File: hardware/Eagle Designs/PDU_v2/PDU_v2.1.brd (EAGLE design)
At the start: 90.2 x 95.5 mm, 245 parts, among them J1 5037630291, J10 5037630491, J11 UJ31-CH-G1-SMT-TR, J12 5037630291, J13 5037630291, J14 5037630291, J15 5037630291, J16 5037630291, J17 5037630291, J18 5037630491, J19 5037630291, J2 5037630291, J20 503182-1852, J22 5037630291, J23 5037630291, J24 5037630291, J25 5037630291, J27 5037630691, J3 5037630291, J4 5037630291, J5 5037630291, J6 5037630291, J7 5037630491, J8 5037630491, J9 5037630491, M1 BSZ100N06LS3, M2 BSZ100N06LS3, M3 BSZ033NE2LS5, M4 BSZ033NE2LS5, U1 DRV8847PWPR, U10 AO3404A, U11 IRLML2803PBFCT-ND, U12 IRLML2803PBFCT-ND, U13 LT8390EFE#PBF, U14 ATSAME51N19A-AF, U15 INA219BIDR, U16 MIC2514YM5-TR, U17 MAX16998AAUA+T, U18 TMP36FSZ, U2 DRV8847PWPR, U20 AO3404A, U21 LT8609A, U22 LT8609A, U23 BC848ALT1G, U24 AO3404A, U25 SI4835DDY-T1-GE3, U26 SI3493DDV-T1-GE3, U27 SI3493DDV-T1-GE3, U3 LTC1477CS8LINEAR_TECHNOLOGY_L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, U4 LTC1477CS8LINEAR_TECHNOLOGY_L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, U5 LTC1477CS8LINEAR_TECHNOLOGY_L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, U6 LTC1477CS8LINEAR_TECHNOLOGY_L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, U7 LTC1477CS8LINEAR_TECHNOLOGY_L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, U8 LT8609A, U9 LTC1477CS8LINEAR_TECHNOLOGY_L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, Y1 ABS07-32.768KHZ-T

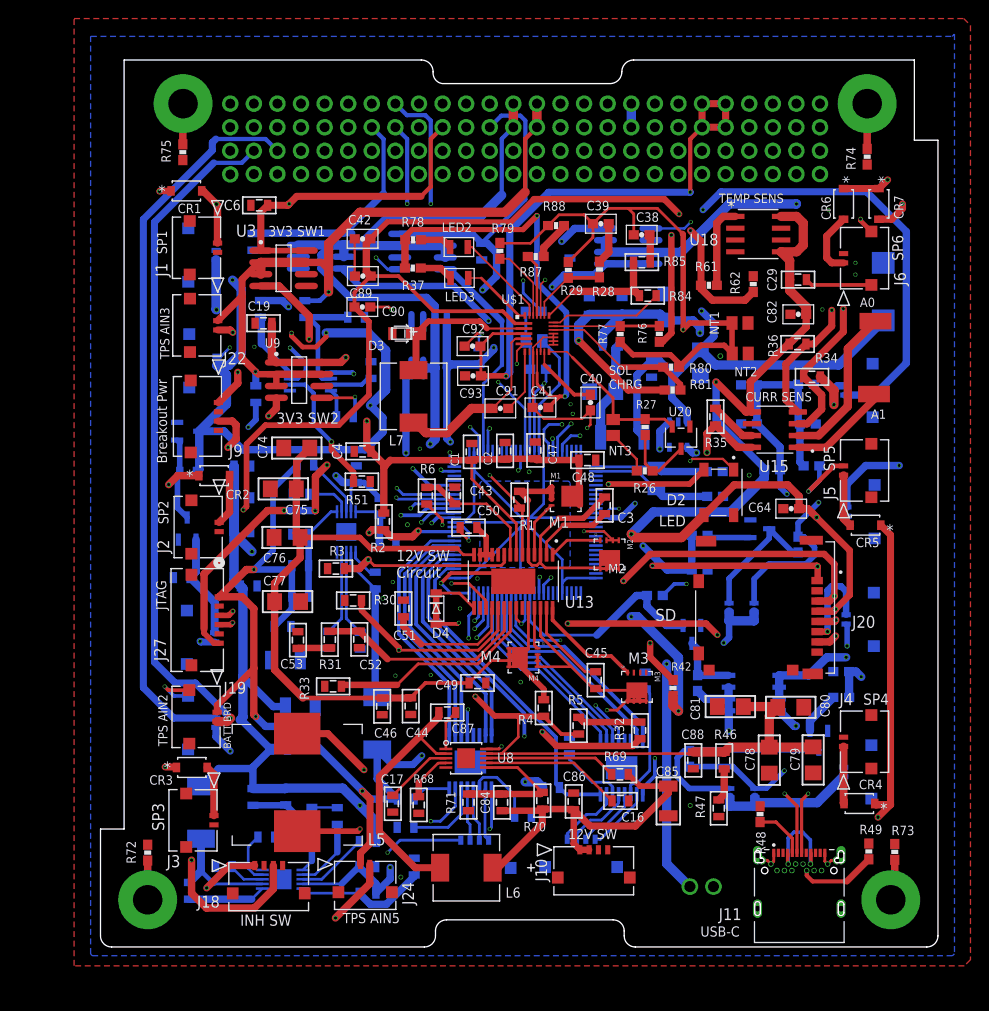
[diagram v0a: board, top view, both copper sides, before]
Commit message: Completed OBC v4.1 (Finished); Updated PDU v2.1 (Unfinished)
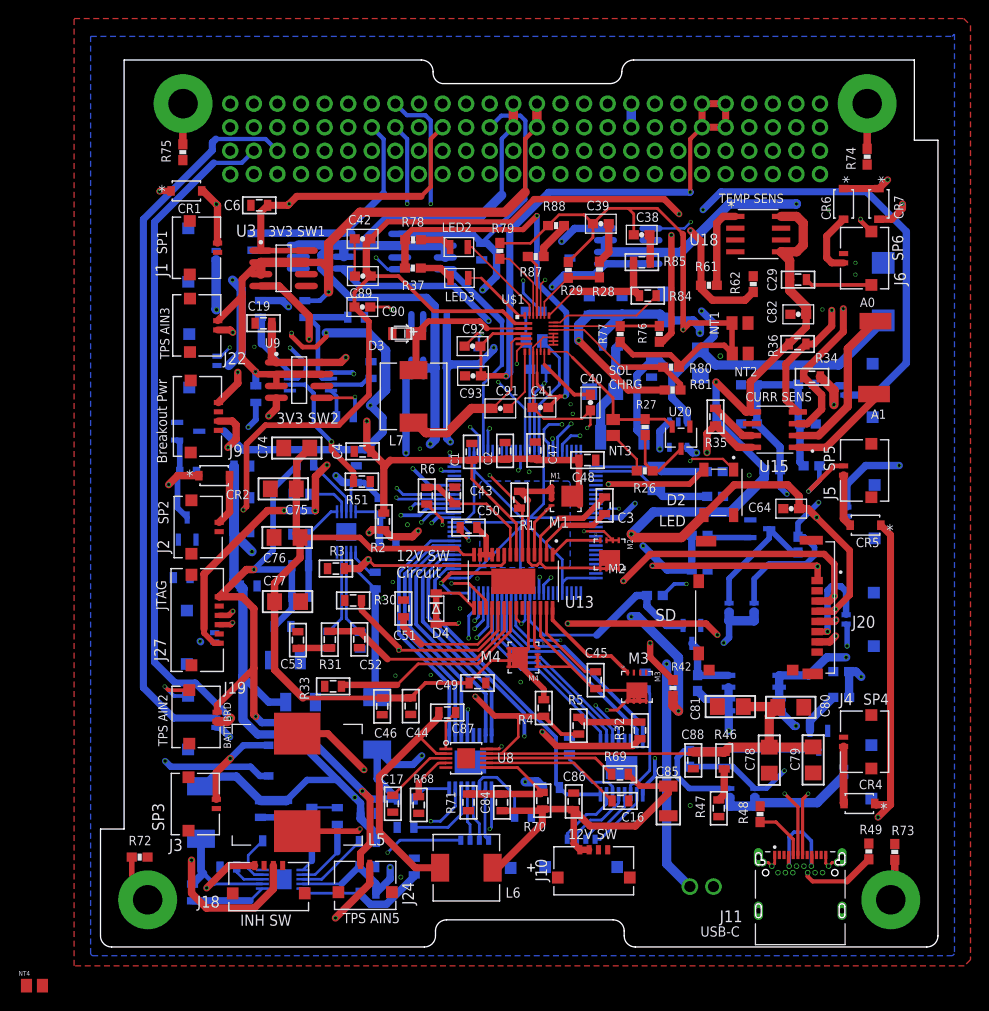
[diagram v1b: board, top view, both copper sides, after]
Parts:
- added NT4: AIMC-0805-2N2S-T, PDUv2:INDC2012X105N
- R15: value 301 k -> 309 k
- R23: value 180 k -> 187 k
- R61: value 27 k -> 45.3 k
- moved C100 11.9 mm to (28.9, 14.4)
- moved CR3 8.31 mm to (18.1, 20.1), flipped to the bottom, turned to 90 degrees
- moved J3 1.77 mm to (12.5, 15.9)
- moved C35 1.53 mm to (17.2, 14.9)
- moved R25 1.32 mm to (20.0, 14.9)
- moved R72 0.99 mm to (4.22, 9.68), turned to 180 degrees
- moved R22 0.65 mm to (18.4, 11.4)
- moved C32 0.49 mm to (13.8, 8.61)
- moved C36 0.48 mm to (21.5, 26.4)
- moved C33 0.38 mm to (9.91, 5.87)
- moved J11 0.25 mm to (72.6, 9.91)
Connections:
- removed net RBF_OUT: J15.2, R83.1, U10.1
- new net PY_VBATT: J15.1, J16.1, R82.2, R83.1, U10.1, U24.3
- new net RBF_GND: NT4.2, R83.2, U10.2
- net GND: now also NT4.1; no longer R83.2, U10.2, U24.2
- net SW_12V_EN1: no longer U14.61
- net VBATT: now also J15.2, U24.2; no longer J15.1, J16.1, R82.2, U24.3
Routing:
- net VBATT: track 336.0 -> 319.4 mm
- net RBF_OUT: track 11.4 -> 0.00 mm
- net INH_SW1_COM: track 275.7 -> 286.3 mm
- net BUS_5V: track 300.8 -> 306.8 mm
- net SOLAR_IN3: track 5.49 -> 9.74 mm, vias 0 -> 1
- net SW_12V_EN1: track 64.8 -> 61.0 mm
- net BUS_3V3: track 407.6 -> 405.1 mm
- net BUS_5V_FB: track 12.6 -> 11.2 mm
- net N$59: track 4.23 -> 5.31 mm
- net USB_D+: track 131.8 -> 132.4 mm
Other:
- board text added: "C:/Users/kelly/Downloads/ARTEMIS logo stencil.bmp"
- board text added: "C:/Users/kelly/Downloads/official.bmp"
- board text added: "PDU v2.1"
